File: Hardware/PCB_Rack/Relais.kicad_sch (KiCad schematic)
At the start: 6 parts, among them J2 Conn_01x03, Q1 SQ2310ES-T1_BE3, Q2 SQ2310ES-T1_BE3

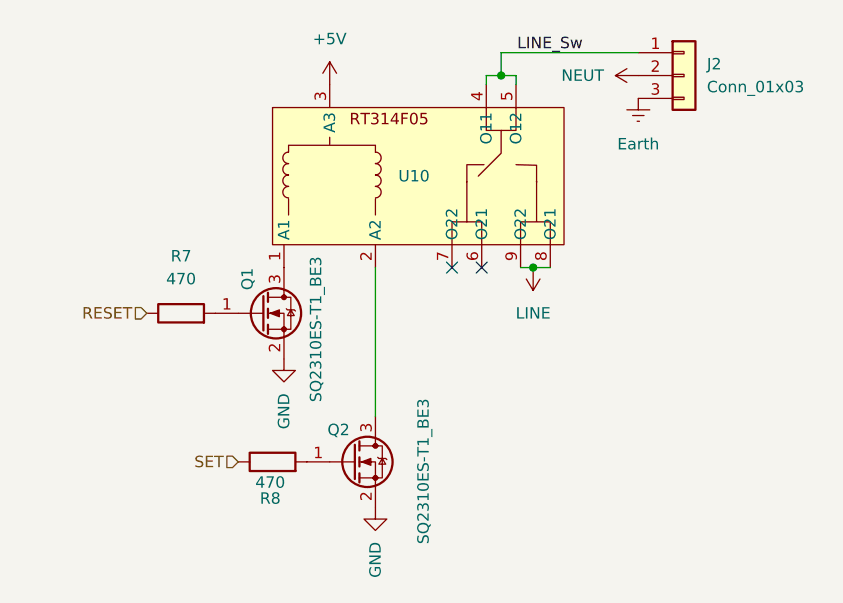
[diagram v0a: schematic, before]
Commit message: ajout des pulldown sur les transistors
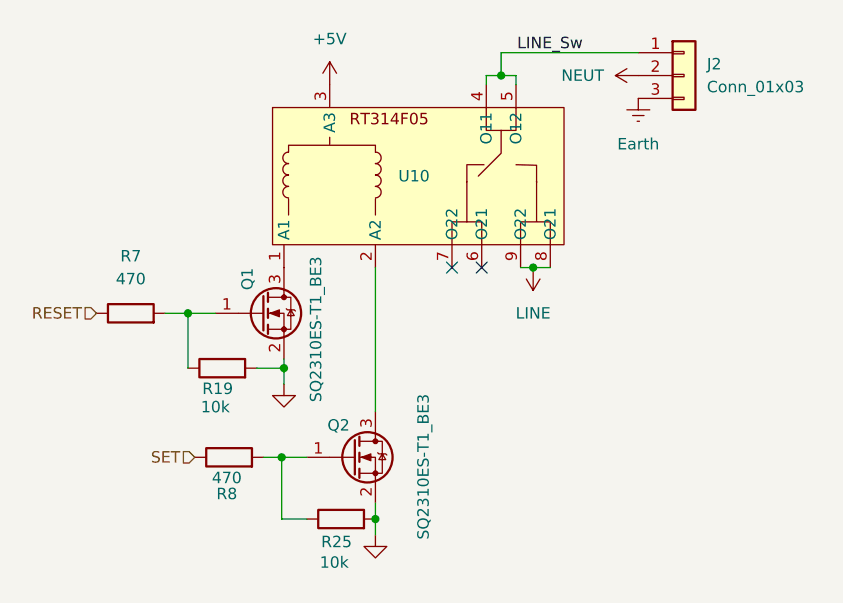
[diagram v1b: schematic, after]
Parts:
- added R19, R25: 10k, Resistor_SMD:R_0603_1608Metric_Pad0.98x0.95mm_HandSolder, symbol Device:R
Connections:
- net GND: now also R19.2, R25.2
- net at Q2.1 (G), R8.2: now also R25.1
- net at Q1.1 (G), R7.2: now also R19.1
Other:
- moved on the sheet: Q2, R7, R8

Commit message: ajout des pinheaders en plus
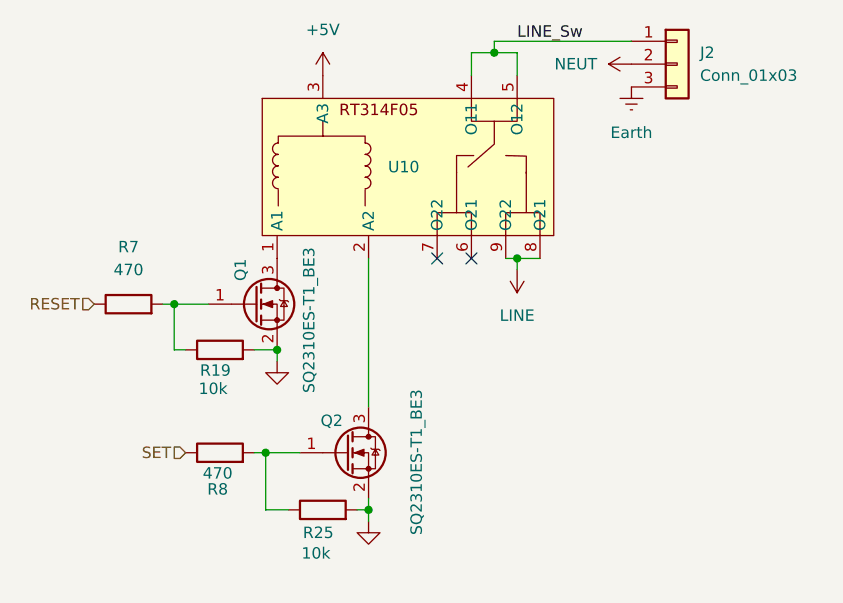
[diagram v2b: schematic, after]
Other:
- moved on the sheet: J2, Q1, Q2, R19, R25, R7, R8, U10

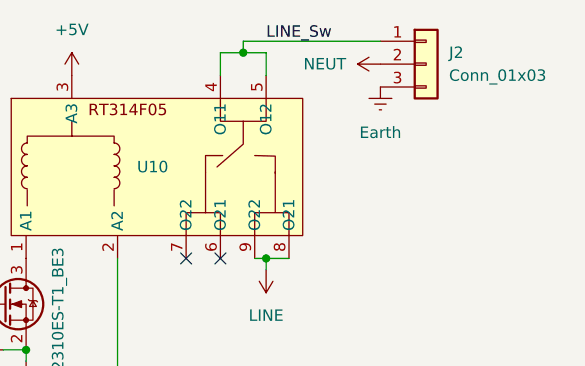
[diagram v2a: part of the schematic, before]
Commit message: correction orientation des connecteurs sur secteur
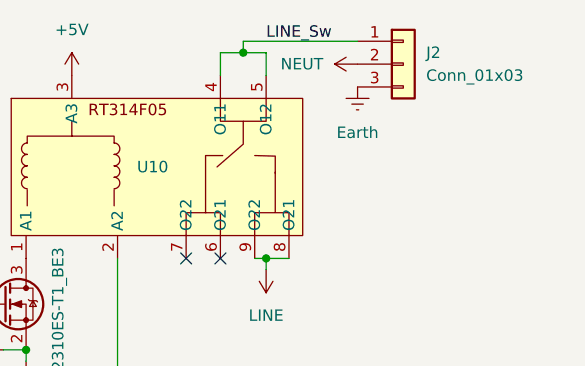
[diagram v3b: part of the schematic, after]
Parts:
- U10: MPN (none) -> RT314F05
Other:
- moved on the sheet: J2
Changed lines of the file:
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@@
+	(wire
+		(pts
+			(xy 156.21 55.88) (xy 168.91 55.88)
+		)
+		(stroke
+			(width 0)
+			(type default)
+		)
+	)
 	(wire
 		(pts
@@
 		(pts
 			(xy 142.24 106.68) (xy 142.24 107.95)
-		)
-		(stroke
-			(width 0)
-			(type default)
-		)
-	)
-	(wire
-		(pts
-			(xy 156.21 55.88) (xy 171.45 55.88)
 		)
 		(stroke
@@
 			)
 		)
-		(property "Datasheet" ""
+		(property "Datasheet" "https://eu.mouser.com/datasheet/2/418/5/ENG_DS_RT1_bistable_0819-728100.pdf"
 			(at 155.575 88.9 0)
 			(effects
@@
 			)
 		)
-		(property "Description" ""
+		(property "Description" "Relais SPDT bistable, 1 from C"
 			(at 155.575 88.9 0)
+			(effects
+				(font
+					(size 1.27 1.27)
+				)
+				(hide yes)
+			)
+		)
+		(property "MPN" "RT314F05"
+			(at 146.05 69.85 0)
 			(effects
 				(font
@@
 	(symbol
 		(lib_id "Connector_Generic:Conn_01x03")
-		(at 176.53 58.42 0)
+		(at 173.99 58.42 0)
 		(unit 1)
 		(exclude_from_sim no)
@@
 		(fields_autoplaced yes)
 		(property "Reference" "J2"
-			(at 179.07 57.1499 0)
+			(at 176.53 57.1499 0)
 			(effects
 				(font
@@
 		)
 		(property "Value" "Conn_01x03"
-			(at 179.07 59.6899 0)
+			(at 176.53 59.6899 0)
 			(effects
 				(font
@@
 		)
 		(property "Footprint" "Conn_Alim:Conn_Secteur_femelle"
-			(at 176.53 58.42 0)
+			(at 173.99 58.42 0)
 			(effects
 				(font
@@
 		)
 		(property "Datasheet" "~"
-			(at 176.53 58.42 0)
+			(at 173.99 58.42 0)
 			(effects
 				(font
@@
 		)
 		(property "Description" "Generic connector, single row, 01x03, script generated (kicad-library-utils/schlib/autogen/connector/)"
-			(at 176.53 58.42 0)
+			(at 173.99 58.42 0)
 			(effects
 				(font
@@
 				(path "/24795ffd-bac6-477a-a38e-d8501482d995/d6311d45-f513-4dac-bbb5-f801c07c799f"
 					(reference "J7")
-					(unit 1)
-				)
-			)
-		)
-	)
-	(symbol
-		(lib_id "power:NEUT")
-		(at 171.45 58.42 90)
-		(unit 1)
-		(exclude_from_sim no)
-		(in_bom yes)
-		(on_board yes)
-		(dnp no)
-		(fields_autoplaced yes)
-		(property "Reference" "#PWR040"
-			(at 175.26 58.42 0)
-			(effects
-				(font
-					(size 1.27 1.27)
-				)
-				(hide yes)
-			)
-		)
-		(property "Value" "NEUT"
-			(at 167.64 58.4199 90)
-			(effects
-				(font
-					(size 1.27 1.27)
-				)
-				(justify left)
-			)
-		)
-		(property "Footprint" ""
-			(at 171.45 58.42 0)
-			(effects
-				(font
-					(size 1.27 1.27)
-				)
-				(hide yes)
-			)
-		)
-		(property "Datasheet" ""
-			(at 171.45 58.42 0)
-			(effects
-				(font
-					(size 1.27 1.27)
-				)
-				(hide yes)
-			)
-		)
-		(property "Description" "Power symbol creates a global label with name \"NEUT\""
-			(at 171.45 58.42 0)
-			(effects
-				(font
-					(size 1.27 1.27)
-				)
-				(hide yes)
-			)
-		)
-		(pin "1"
-		)
-		(instances
-			(project "PCB_Rack"
-				(path "/24795ffd-bac6-477a-a38e-d8501482d995/5442e838-22b7-4759-82c9-b29dca855bd1"
-					(reference "#PWR040")
-					(unit 1)
-				)
-				(path "/24795ffd-bac6-477a-a38e-d8501482d995/5e4c1706-e559-4546-9182-b23e927581d6"
-					(reference "#PWR058")
-					(unit 1)
-				)
-				(path "/24795ffd-bac6-477a-a38e-d8501482d995/75b15100-946d-4ab0-a7ee-fd42b4c9e313"
-					(reference "#PWR052")
-					(unit 1)
-				)
-				(path "/24795ffd-bac6-477a-a38e-d8501482d995/8b3a903d-fead-4375-b5bf-423b54a60210"
-					(reference "#PWR046")
-					(unit 1)
-				)
-				(path "/24795ffd-bac6-477a-a38e-d8501482d995/b42fd1b5-6c7b-4805-bf9d-9efb210f2cb8"
-					(reference "#PWR064")
-					(unit 1)
-				)
-				(path "/24795ffd-bac6-477a-a38e-d8501482d995/d6311d45-f513-4dac-bbb5-f801c07c799f"
-					(reference "#PWR070")
 					(unit 1)
 				)
@@
 	(symbol
 		(lib_id "power:Earth")
-		(at 171.45 60.96 0)
+		(at 168.91 60.96 0)
 		(unit 1)
 		(exclude_from_sim no)
@@
 		(fields_autoplaced yes)
 		(property "Reference" "#PWR041"
-			(at 171.45 67.31 0)
+			(at 168.91 67.31 0)
 			(effects
 				(font
@@
 		)
 		(property "Value" "Earth"
-			(at 171.45 66.04 0)
+			(at 168.91 66.04 0)
 			(effects
 				(font
@@
 		)
 		(property "Footprint" ""
-			(at 171.45 60.96 0)
+			(at 168.91 60.96 0)
 			(effects
 				(font
@@
 		)
 		(property "Datasheet" "~"
-			(at 171.45 60.96 0)
+			(at 168.91 60.96 0)
 			(effects
 				(font
@@
 		)
 		(property "Description" "Power symbol creates a global label with name \"Earth\""
-			(at 171.45 60.96 0)
+			(at 168.91 60.96 0)
 			(effects
 				(font
@@
 					(unit 1)
 				)
+			)
+		)
+	)
+	(symbol
+		(lib_id "power:NEUT")
+		(at 168.91 58.42 90)
+		(unit 1)
+		(exclude_from_sim no)
+		(in_bom yes)
+		(on_board yes)
+		(dnp no)
+		(fields_autoplaced yes)
+		(property "Reference" "#PWR046"
+			(at 172.72 58.42 0)
+			(effects
+				(font
+					(size 1.27 1.27)
+				)
+				(hide yes)
+			)
+		)
+		(property "Value" "NEUT"
+			(at 165.1 58.4199 90)
+			(effects
+				(font
+					(size 1.27 1.27)
+				)
+				(justify left)
+			)
+		)
+		(property "Footprint" ""
+			(at 168.91 58.42 0)
+			(effects
+				(font
+					(size 1.27 1.27)
+				)
+				(hide yes)
+			)
+		)
+		(property "Datasheet" ""
+			(at 168.91 58.42 0)
+			(effects
+				(font
+					(size 1.27 1.27)
+				)
+				(hide yes)
+			)
+		)
+		(property "Description" "Power symbol creates a global label with name \"NEUT\""
+			(at 168.91 58.42 0)
+			(effects
+				(font
+					(size 1.27 1.27)
+				)
+				(hide yes)
+			)
+		)
+		(pin "1"
+		)
+		(instances
+			(project "PCB_Rack"
+				(path "/24795ffd-bac6-477a-a38e-d8501482d995/5442e838-22b7-4759-82c9-b29dca855bd1"
+					(reference "#PWR046")
+					(unit 1)
+				)
+				(path "/24795ffd-bac6-477a-a38e-d8501482d995/5e4c1706-e559-4546-9182-b23e927581d6"
+					(reference "#PWR057")
+					(unit 1)
+				)
+				(path "/24795ffd-bac6-477a-a38e-d8501482d995/75b15100-946d-4ab0-a7ee-fd42b4c9e313"
+					(reference "#PWR052")
+					(unit 1)
+				)
+				(path "/24795ffd-bac6-477a-a38e-d8501482d995/8b3a903d-fead-4375-b5bf-423b54a60210"
+					(reference "#PWR051")
+					(unit 1)
+				)
+				(path "/24795ffd-bac6-477a-a38e-d8501482d995/b42fd1b5-6c7b-4805-bf9d-9efb210f2cb8"
+					(reference "#PWR058")
+					(unit 1)
+				)
+				(path "/24795ffd-bac6-477a-a38e-d8501482d995/d6311d45-f513-4dac-bbb5-f801c07c799f"
+					(reference "#PWR064")
+					(unit 1)
+				)
